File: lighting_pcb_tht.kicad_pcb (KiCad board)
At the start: 2 copper layers, 41 x 50 mm, 20 parts, among them J1 Screw_Terminal_01x03, SW1 SW_Push, SW2 SW_Push, SW3 SW_Push, U1 ATmega328-P, Y1 Crystal

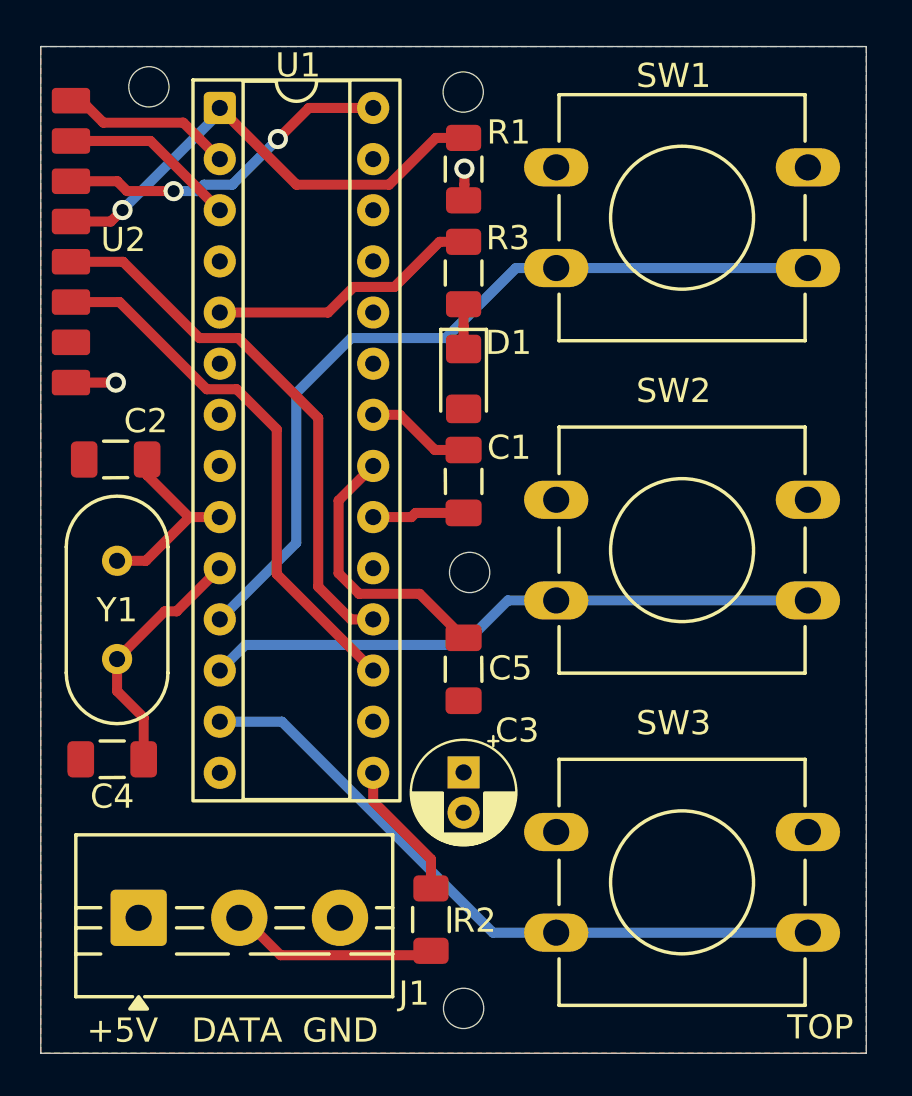
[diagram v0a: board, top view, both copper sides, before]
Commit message: Changed the pads used for programming to header pins
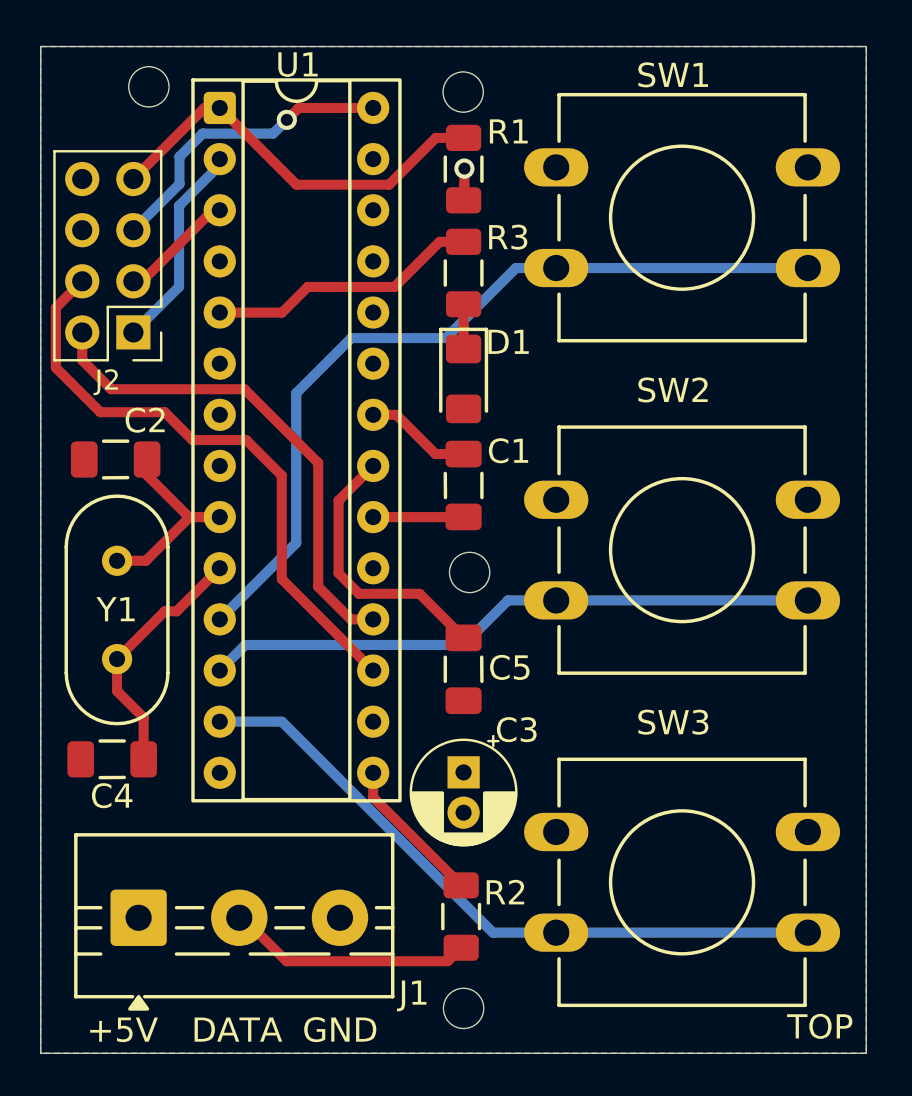
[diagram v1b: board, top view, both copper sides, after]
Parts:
- removed U2: ~, Programming_Pad:Programming_Pad
- added J2: Conn_02x04_Odd_Even, Connector_PinHeader_2.54mm:PinHeader_2x04_P2.54mm_Vertical, F.Cu at (4.60, 14.2)
- moved R2 1.51 mm to (20.9, 43.2)
- moved C1 0.20 mm to (21.0, 21.8)
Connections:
- U1 pad 14: Net-(U1-PB0) -> unconnected-(U1-PB0-Pad14)
- U1 pad 16: Net-(U1-PB2) -> unconnected-(U1-PB2-Pad16)
- U1 pad 19: Net-(U1-PB5) -> unconnected-(U1-PB5-Pad19)
- U1 pad 24: Net-(U1-PC1) -> unconnected-(U1-PC1-Pad24)
- U1 pad 26: Net-(U1-PC3) -> unconnected-(U1-PC3-Pad26)
- U1 pad 4: Net-(U1-PD2) -> unconnected-(U1-PD2-Pad4)
- U1 pad 6: Net-(U1-PD4) -> unconnected-(U1-PD4-Pad6)
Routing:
- net Net-(J2-Pin_7): track 24.5 -> 20.6 mm, vias 1 -> 0
- net Net-(J2-Pin_3): track 8.81 -> 5.75 mm
- net Net-(J2-Pin_4): track 26.8 -> 29.8 mm
- net Net-(J2-Pin_2): track 27.3 -> 24.8 mm
- net +5V: track 9.19 -> 6.88 mm, vias 2 -> 1
- net Net-(J1-Pin_2): track 10.5 -> 12.3 mm
- net Net-(J2-Pin_1): track 8.59 -> 10.4 mm
- net Net-(J2-Pin_5): track 16.9 -> 15.2 mm, vias 2 -> 1

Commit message: Final design with THT chip and SMD res/caps
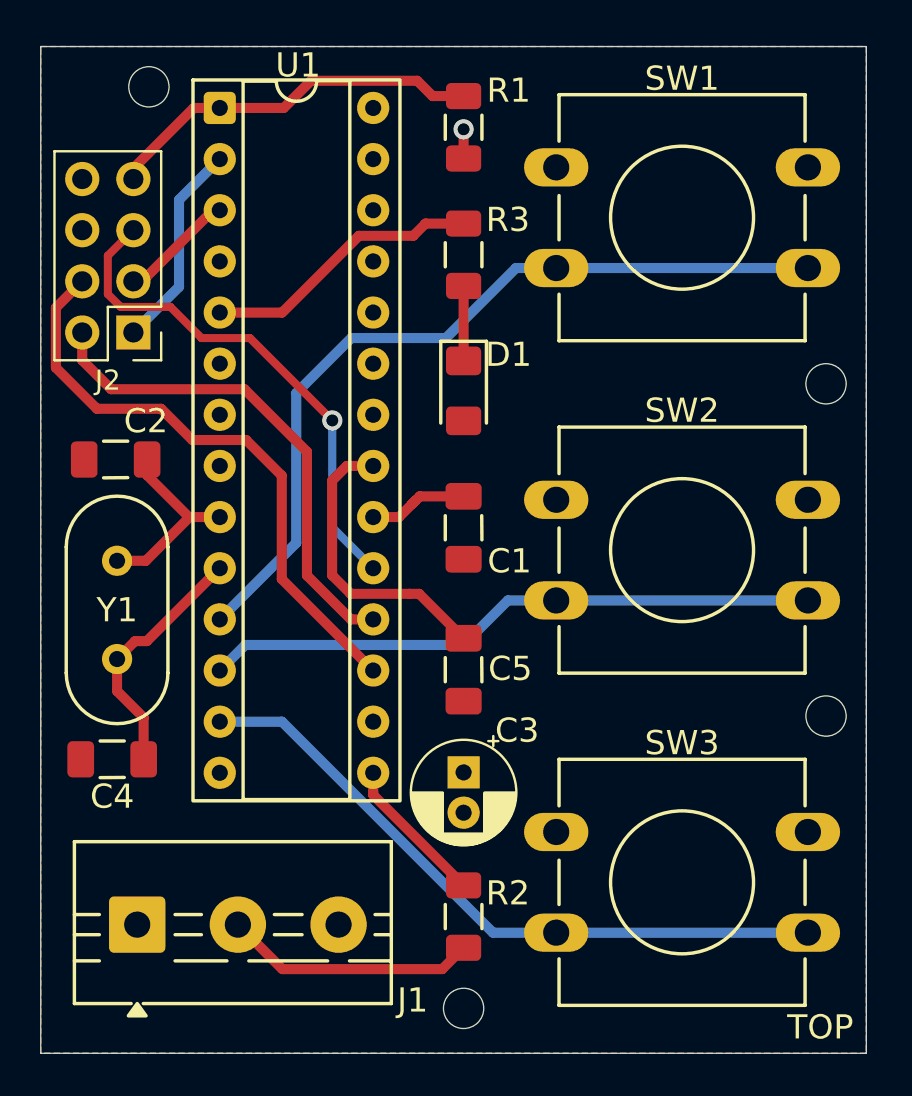
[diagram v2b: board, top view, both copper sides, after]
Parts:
- moved H2 23.1 mm to (39.0, 16.8)
- moved H3 19.1 mm to (39.0, 33.2)
- moved C1 2.10 mm to (21.0, 23.9), turned to -90 degrees
- moved R1 2.08 mm to (21.0, 4.01)
- moved R3 0.91 mm to (21.0, 10.3)
- moved D1 0.59 mm to (21.0, 17.1)
- moved J1 0.35 mm to (4.79, 43.6)
- moved R2 0.12 mm to (21.0, 43.2)
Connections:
- J1 pad 1: +5V -> GND
- J1 pad 3: GND -> +5V
- U1 pad 19: unconnected-(U1-PB5-Pad19) -> Net-(J2-Pin_5)
- U1 pad 27: +5V -> unconnected-(U1-PC4-Pad27)
- U1 pad 28: Net-(J2-Pin_5) -> unconnected-(U1-PC5-Pad28)
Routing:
- net Net-(J2-Pin_5): track 15.2 -> 25.6 mm
- net GND: track 5.30 -> 0.00 mm
- net Net-(J2-Pin_7): track 20.6 -> 19.3 mm
- net Net-(U1-AREF): track 13.6 -> 14.9 mm
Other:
- board text added: "MISO"
- board text added: "MOSI"
- board text added: "RST"
- board text added: "RX"
- board text added: "SCK"
- board text added: "TX"
